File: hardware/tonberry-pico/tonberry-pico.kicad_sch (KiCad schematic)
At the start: 30 parts, among them J1 MicroSD_Breakout, J2 SparkFun I2S Audio Breakout M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, J3 RC522_Breakout, J4 Adafruit_bq25185_5V, J5 UART, J6 WS2812, J7 Buttons, J8 Conn_01x01, Q1 2N7000, Q2 2N7000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

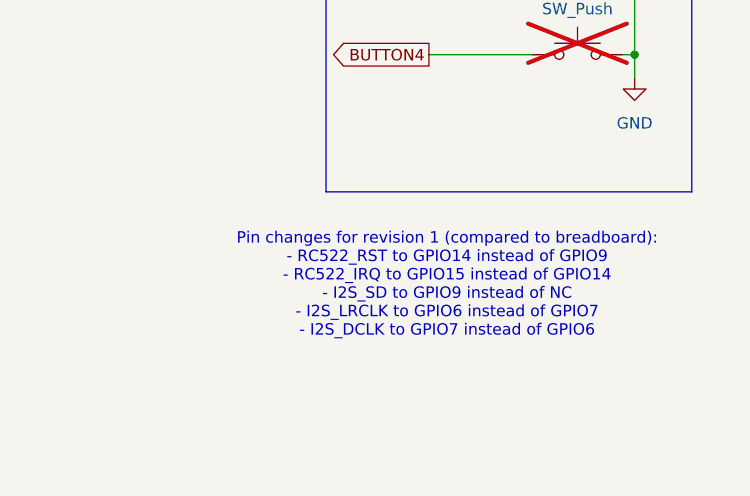
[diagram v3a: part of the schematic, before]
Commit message: hw: Update metadata, move silkscreen board name + rev
No netlist or routing changes.

Signed-off-by: Matthias Blankertz <matthias@blankertz.org>
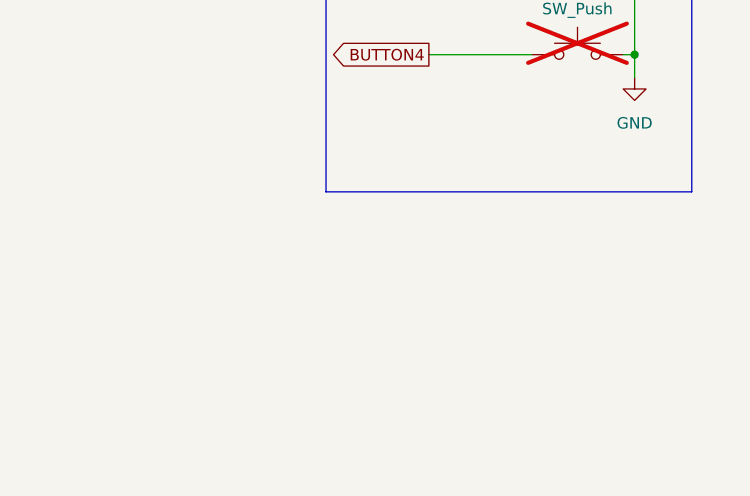
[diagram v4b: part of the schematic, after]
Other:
- note removed: "Pin changes for revision 1 (compared to breadboard): - RC522_RST to GPIO14 instead of GPIO9 - RC522_IRQ to GPIO15 instead of GPIO14 - I2S_SD to GPIO9 instead of NC - I2S_LRCLK to GPIO6 instead of GPIO7 - I2S_DCLK to GPIO7 instead of GPIO6"
- title: (none) -> Tonberry Pico
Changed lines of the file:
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@@
 	(generator_version "9.0")
 	(paper "A4")
+	(title_block
+		(title "Tonberry Pico")
+		(date "2025-11-08")
+		(rev "1.2")
+		(comment 1 "Copyright (c) 2025 Matthias Blankertz <matthias@blankertz.org>")
+		(comment 2 "SPDX-License-Identifier: MIT")
+	)
 	(rectangle
 		(start 14.478 109.728)
@@
 			)
 		)
-	)
-	(text "Pin changes for revision 1 (compared to breadboard):\n- RC522_RST to GPIO14 instead of GPIO9\n- RC522_IRQ to GPIO15 instead of GPIO14\n- I2S_SD to GPIO9 instead of NC\n- I2S_LRCLK to GPIO6 instead of GPIO7\n- I2S_DCLK to GPIO7 instead of GPIO6"
-		(exclude_from_sim no)
-		(at 256.032 174.244 0)
-		(effects
-			(font
-				(size 1.27 1.27)
-			)
-		)

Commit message: hw: Final fixes for Rev 1.2
- Move RC522 connector a bit further away from the MAX98375 module
  footprint, so a JST-XH connector can be used here too.
- Update custom rules and fix some DRC warnings (no netlist and layout
  changes).

Signed-off-by: Matthias Blankertz <matthias@blankertz.org>
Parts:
- J8: now left out of the parts list
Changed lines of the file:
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@@
 		(unit 1)
 		(exclude_from_sim no)
-		(in_bom yes)
+		(in_bom no)
 		(on_board yes)
 		(dnp no)
